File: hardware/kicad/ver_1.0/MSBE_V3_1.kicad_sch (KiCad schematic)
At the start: 88 parts, among them J10 Low-V, J11 USB_C_Receptacle_USB2.0_16P, J12 Touch Pads, J13 UART, J14 Prog, J9 High-V, U10 MAX98357AEWL_T, U11 NPM1100-CAAA-R7, U12 NRF5340-CLAA-R, U13 BMA400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

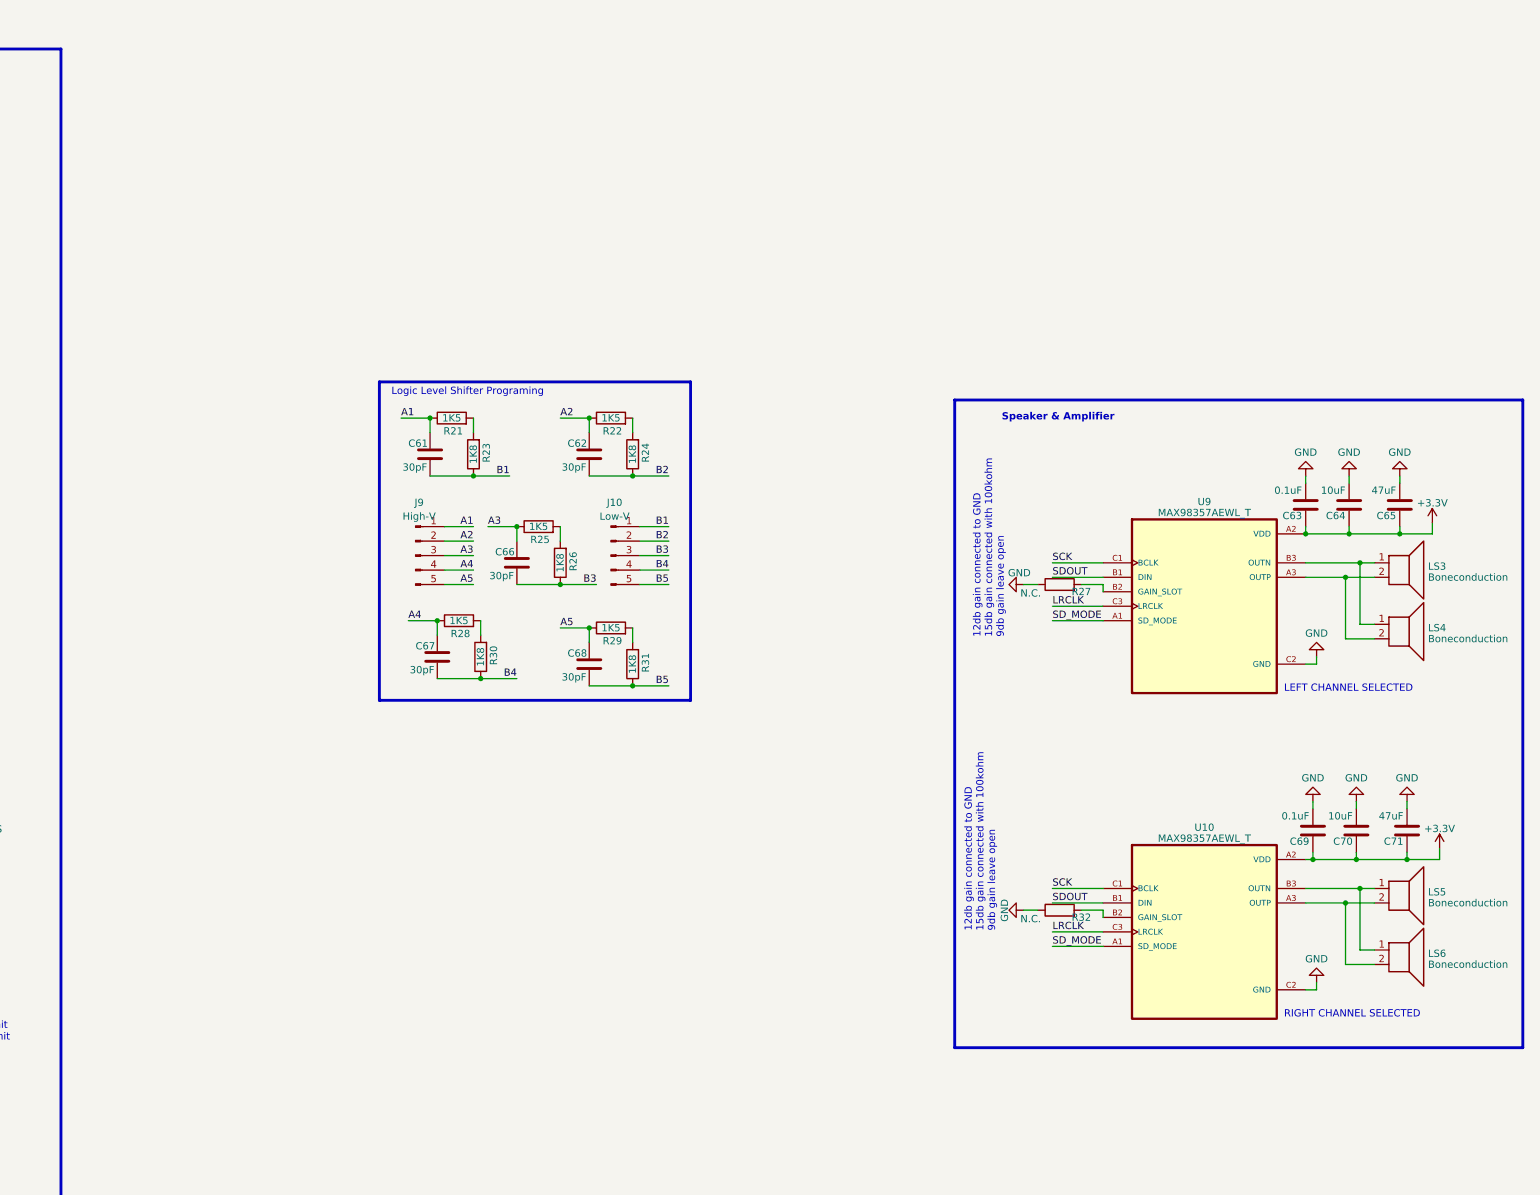
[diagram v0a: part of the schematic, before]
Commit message: updated schematic QFN
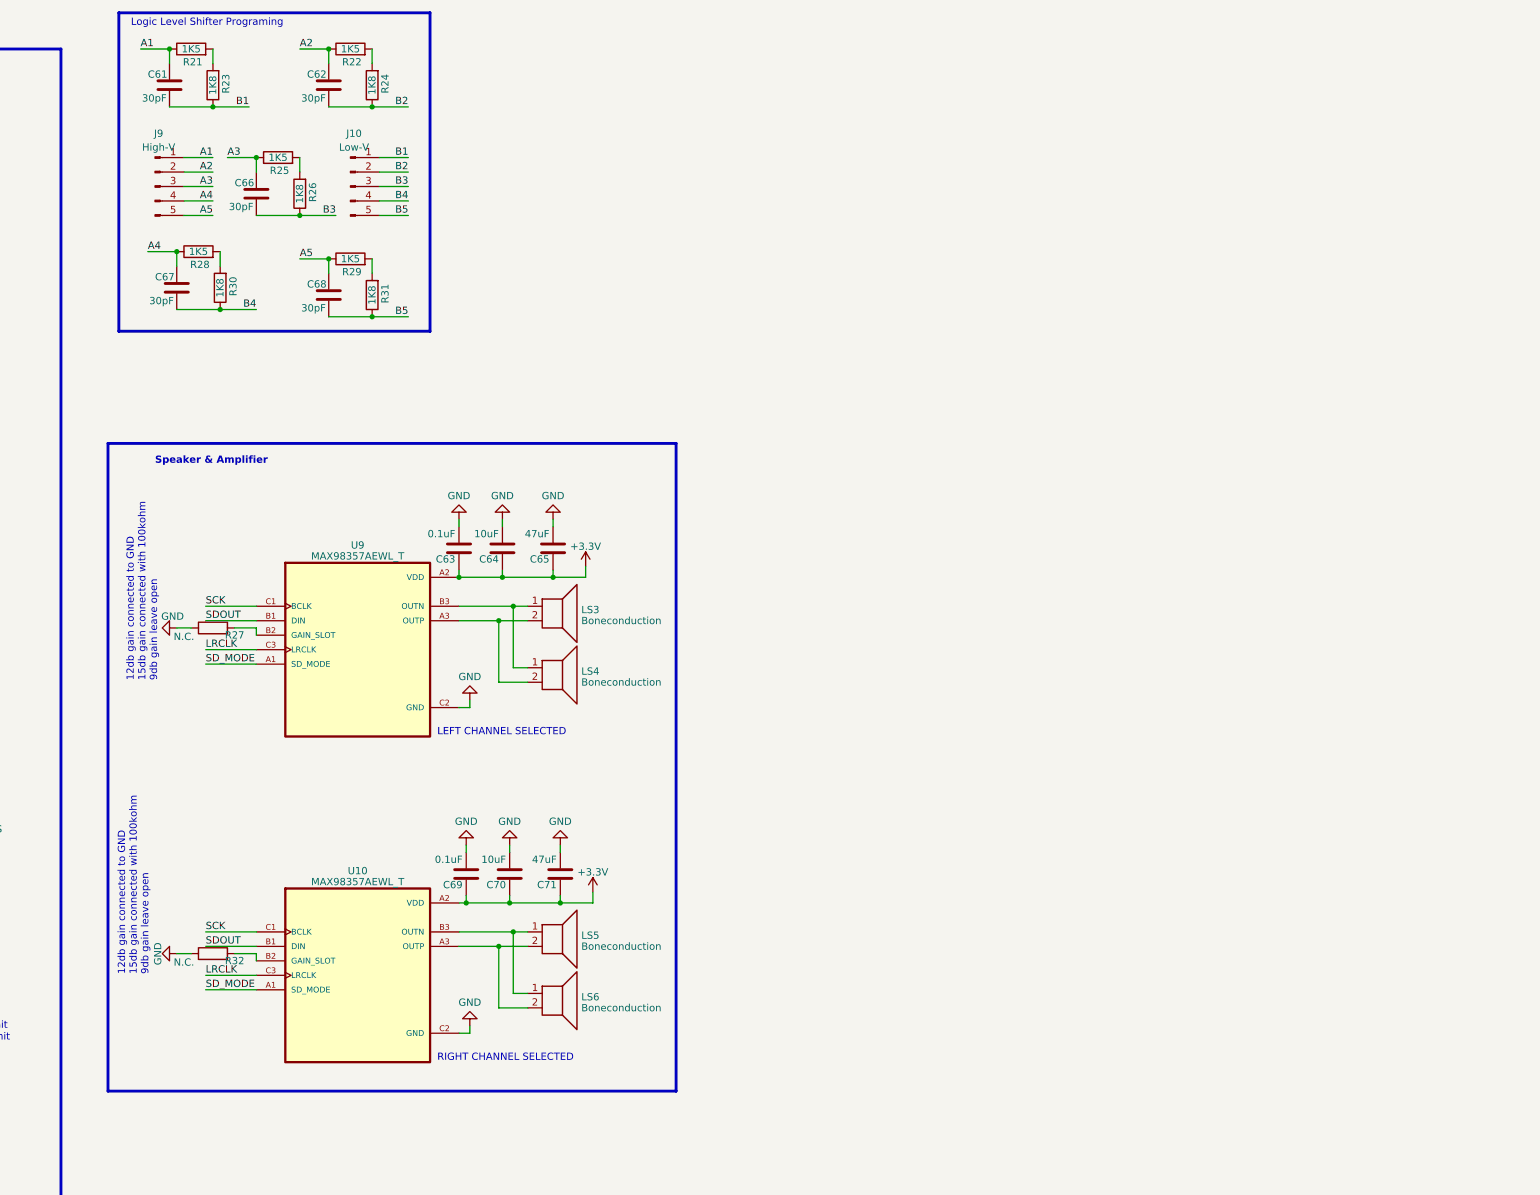
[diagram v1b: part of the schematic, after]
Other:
- moved on the sheet: C61, C62, C63, C64, C65, C66, C67, C68, C69, C70, C71, J10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
